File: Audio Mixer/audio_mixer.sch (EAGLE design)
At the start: 0 parts

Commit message: Audio Mixer half done
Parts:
- added C1, C2, C22, C23, C24, C25, C3, C31, C33, C34, C35, C4, C5, C6, C7, C8: 0.1u, rcl:C-EU025-030X050
- added C10, C11, C12, C9: 10u, rcl:CPOL-EUE5-10.5
- added C13, C14: 15n, rcl:C-EU025-030X050
- added C15: 100u, rcl:CPOL-EUE5-10.5
- added C16, C19, C20, C21: 2.2u, rcl:CPOL-EUE2.5-6
- added C17, C18: 56n, rcl:C-EU025-030X050
- added C26, C27, C28, C29: 47n, rcl:C-EU025-030X050
- added C30, C32: 1000u, rcl:C-EU050-050X075
- added IC1: LM747H, linear:LM747H
- added R1, R10, R11, R12, R13, R14, R15, R16, R17, R18, R19, R2, R20, R3, R4, R5, R6, R7, R8, R9: (no value), rcl:R-EU_R0805
- added R21, R22, R23, R24, R25, R26, R27, R28, R29, R30: (no value), rcl:POTENTIOMETER_PT-10
- added U1: TDA1524A, TDA1524A:TDA1524A
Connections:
- new net +12V: C11.+, IC1A.V+, IC1B.V+
- new net -12V: C10.-, C9.-, IC1P.V-
- new net AGND: C11.-, C9.+
- new net N$1: C1.1, R1.1
- new net N$10: R1.2, R21.3
- new net N$11: R2.2, R22.3
- new net N$12: R23.3, R3.2
- new net N$13: R24.3, R4.2
- new net N$14: R25.3, R5.2
- new net N$15: R26.3, R6.2
- new net N$16: R27.3, R7.2
- new net N$17: R28.3, R8.2
- new net N$18: C12.+, R10.1, R9.1
- new net N$19: IC1A.OUT, R10.2, R29.3
- new net N$2: C10.+, IC1A.+IN, IC1B.+IN, R21.2, R22.2, R23.2, R24.2, R25.2, R26.2, R27.2, R28.2
- new net N$20: IC1A.-IN, R21.1, R22.1, R23.1, R24.1, R29.1
- new net N$21: IC1B.-IN, R25.1, R26.1, R27.1, R28.1, R30.2
- new net N$22: IC1B.OUT, R30.3, R9.2
- new net N$23: C12.-, U1.LEFT_IN, U1.RIGHT_IN
- new net N$3: C2.1, R2.1
- new net N$4: C3.1, R3.1
- new net N$5: C4.1, R4.1
- new net N$6: C5.1, R5.1
- new net N$7: C6.1, R6.1
- new net N$8: C7.1, R7.1
- new net N$9: C8.1, R8.1

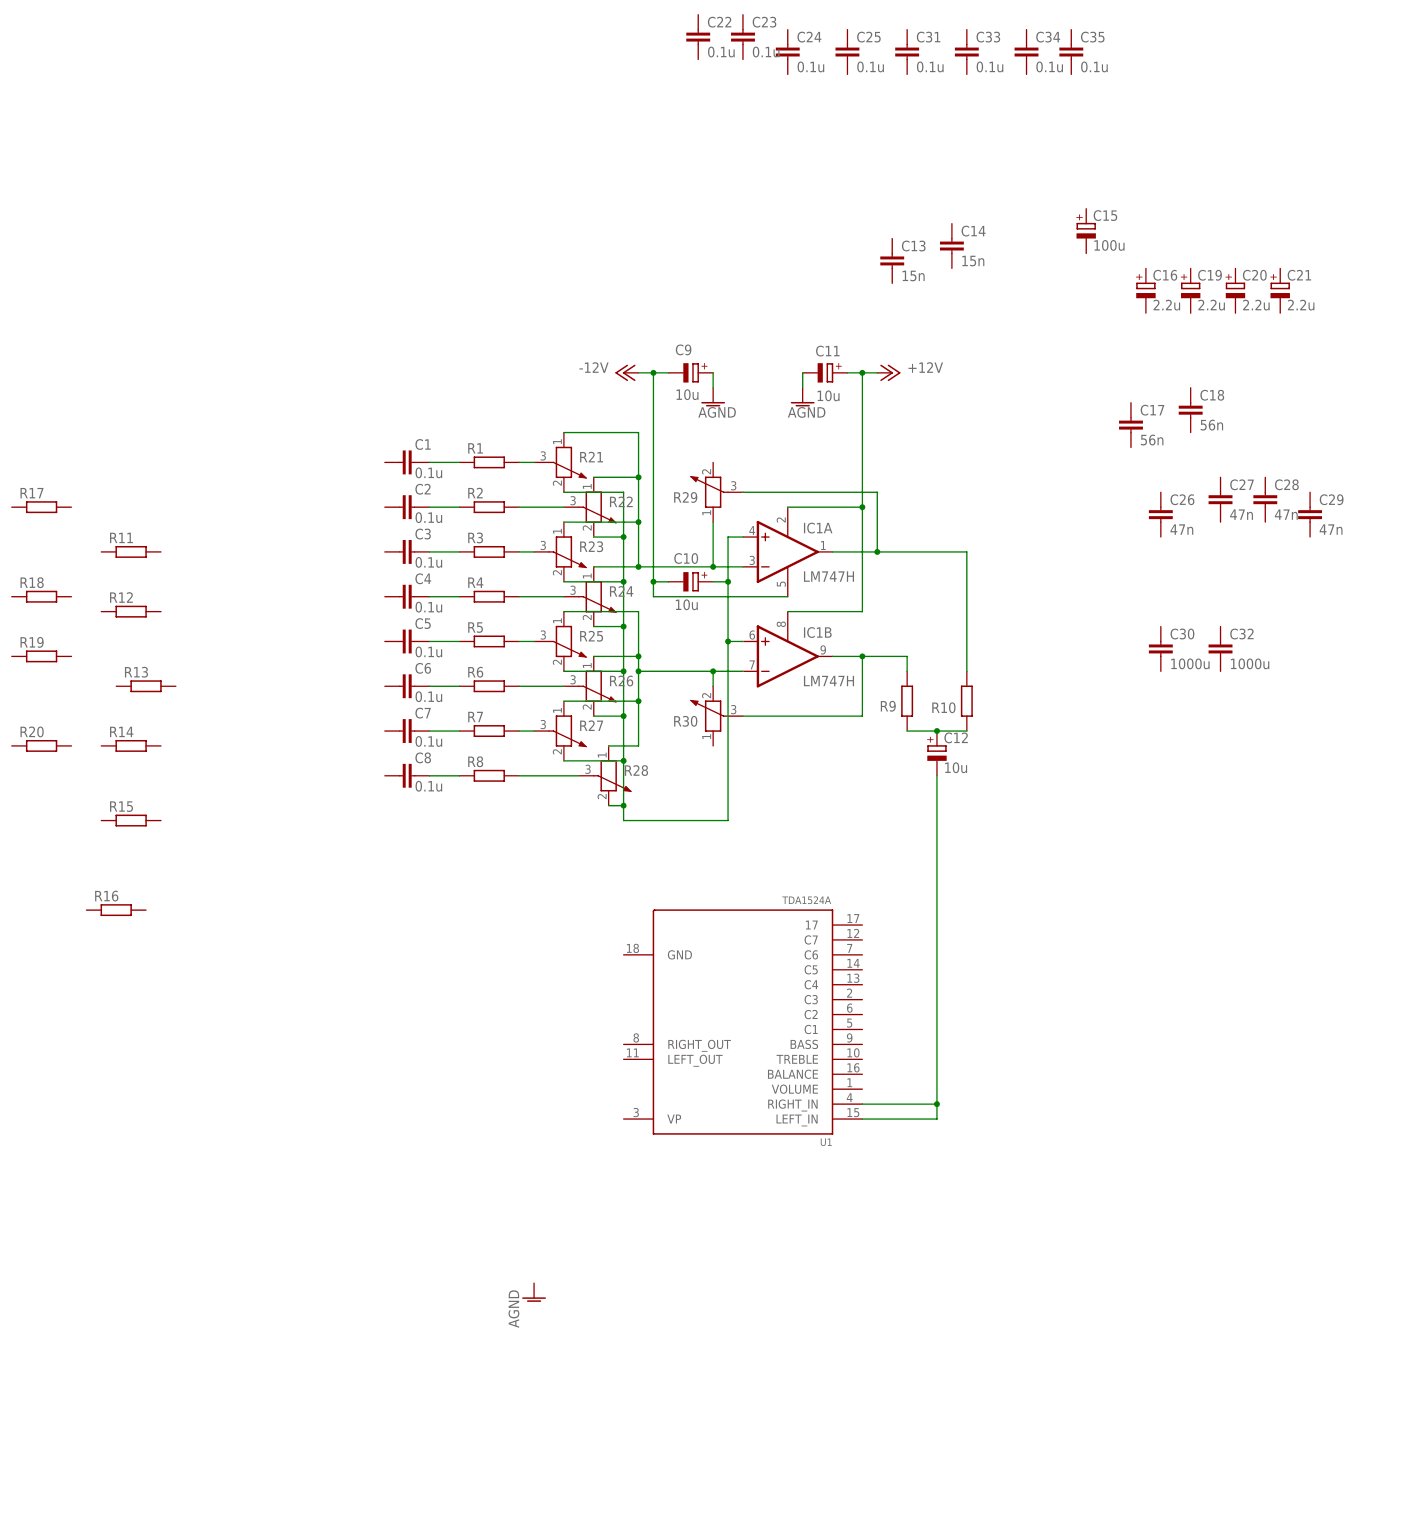
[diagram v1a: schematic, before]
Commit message: mixer schematic functionally done, todo labels and brd
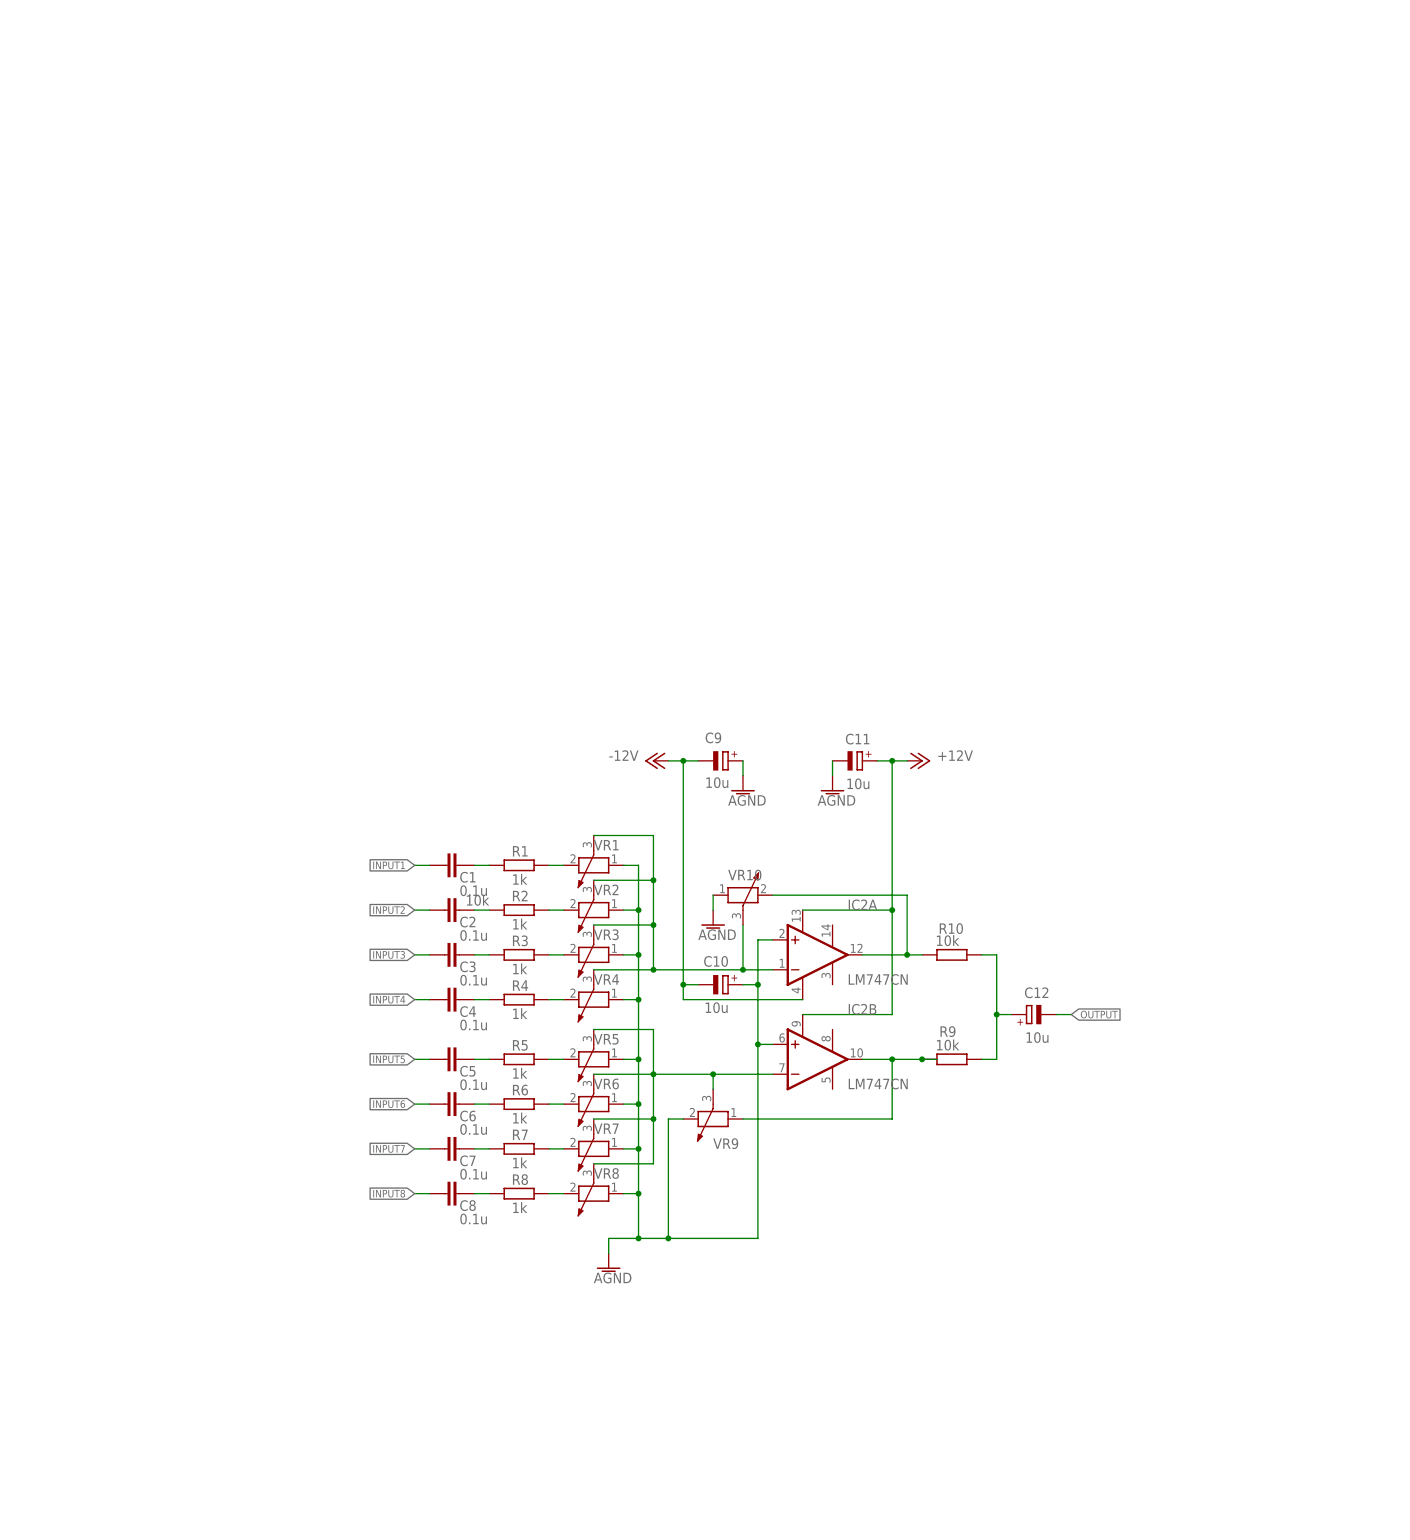
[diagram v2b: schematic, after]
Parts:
- removed C13, C14: 15n, rcl:C-EU025-030X050
- removed C15: 100u, rcl:CPOL-EUE5-10.5
- removed C16, C19, C20, C21: 2.2u, rcl:CPOL-EUE2.5-6
- removed C17, C18: 56n, rcl:C-EU025-030X050
- removed C22, C23, C24, C25, C31, C33, C34, C35: 0.1u, rcl:C-EU025-030X050
- removed C26, C27, C28, C29: 47n, rcl:C-EU025-030X050
- removed C30, C32: 1000u, rcl:C-EU050-050X075
- removed IC1: LM747H, linear:LM747H
- removed R11, R12, R13, R14, R15, R16, R17, R18, R19, R20: (no value), rcl:R-EU_R0805
- removed R21, R22, R23, R24, R25, R26, R27, R28, R29, R30: (no value), rcl:POTENTIOMETER_PT-10
- removed U1: TDA1524A, TDA1524A:TDA1524A
- added IC2: LM747CN, linear:LM747CN
- added VR1: 10k, rcl:POTENTIOMETER_PT-10
- added VR10, VR2, VR3, VR4, VR5, VR6, VR7, VR8, VR9: (no value), rcl:POTENTIOMETER_PT-10
- R1, R2, R3, R4, R5, R6, R7, R8: value (none) -> 1k
- R10, R9: value (none) -> 10k
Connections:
- removed net N$2 (its old number): C10.+, IC1A.+IN, IC1B.+IN, R21.2, R22.2, R23.2, R24.2, R25.2, R26.2, R27.2, R28.2
- removed net N$20: IC1A.-IN, R21.1, R22.1, R23.1, R24.1, R29.1
- removed net N$23: C12.-, U1.LEFT_IN, U1.RIGHT_IN
- new net INPUT1: C1.2
- new net INPUT2: C2.2
- new net INPUT3: C3.2
- new net INPUT4: C4.2
- new net INPUT5: C5.2
- new net INPUT6: C6.2
- new net INPUT7: C7.2
- new net INPUT8: C8.2
- new net N$18: R2.2, VR2.2
- new net OUTPUT: C12.-
- net +12V: now also IC2A.V+, IC2B.V+; no longer IC1A.V+, IC1B.V+
- net -12V: now also IC2P.V-; no longer IC1P.V-
- net AGND: now also C10.+, IC2A.+IN, IC2B.+IN, VR1.1, VR10.1, VR2.1, VR3.1, VR4.1, VR5.1, VR6.1, VR7.1, VR8.1, VR9.2
- net N$10: now also R3.2, VR3.2; no longer R1.2, R21.3
- net N$11: now also IC2B.-IN, VR5.3, VR6.3, VR7.3, VR8.3, VR9.3; no longer R2.2, R22.3
- net N$12: now also IC2A.-IN, VR1.3, VR10.3, VR2.3, VR3.3, VR4.3; no longer R23.3, R3.2
- net N$13: now also R1.2, VR1.2; no longer R24.3, R4.2
- net N$14: now also R4.2, VR4.2; no longer R25.3, R5.2
- net N$15: now also R5.2, VR5.2; no longer R26.3, R6.2
- net N$16: now also R6.2, VR6.2; no longer R27.3, R7.2
- net N$17: now also R7.2, VR7.2; no longer R28.3, R8.2
- net N$19: now also IC2A.OUT, VR10.2; no longer IC1A.OUT, R29.3
- net N$21: now also R8.2, VR8.2; no longer IC1B.-IN, R25.1, R26.1, R27.1, R28.1, R30.2
- net N$22: now also IC2B.OUT, VR9.1; no longer IC1B.OUT, R30.3
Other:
- moved on the sheet: C1, C10, C11, C12, C2, C3, C4, C5, C6, C7, C8, C9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

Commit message: Mixer Design complete
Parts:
- removed IC2: LM747CN, linear:LM747CN
- added C13: 10u, rcl:CPOL-EUE5-10.5
- added C14, C15, C16, C17, C18, C19, C20, C21, C22, C24: 0.1u, rcl:C-EU025-030X050
- added IC1: OPA2134P, linear:OPA2134P
- added INPUT_AUDIO: (no value), pinhead:PINHD-2X9
- added OUTPUT_AUDIO, POWER: (no value), pinhead:PINHD-1X3
- added R11, R12, R13, R14, R15, R16, R17, R18, R19, R21: 1k, rcl:R-EU_R0805
- added VR11, VR16: 10k, rcl:POTENTIOMETER_PT-10
- added VR12, VR13, VR14, VR15, VR17, VR18, VR19, VR21: (no value), rcl:POTENTIOMETER_PT-10
- VR6: value (none) -> 10k
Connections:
- removed net +12V: C11.+, IC2A.V+, IC2B.V+
- removed net -12V: C10.-, C9.-, IC2P.V-
- removed net INPUT1: C1.2
- removed net INPUT2: C2.2
- removed net INPUT3: C3.2
- removed net INPUT4: C4.2
- removed net INPUT5: C5.2
- removed net INPUT6: C6.2
- removed net INPUT7: C7.2
- removed net INPUT8: C8.2
- removed net OUTPUT: C12.-
- new net +15V: C11.+, IC1P.V+, POWER.1
- new net -15V: C10.-, C9.-, IC1P.V-, POWER.2
- new net L_INPUT1: C15.2, INPUT_AUDIO.1
- new net L_INPUT2: C16.2, INPUT_AUDIO.3
- new net L_INPUT3: C17.2, INPUT_AUDIO.5
- new net L_INPUT4: C18.2, INPUT_AUDIO.7
- new net L_INPUT5: C19.2, INPUT_AUDIO.9
- new net L_INPUT6: C20.2, INPUT_AUDIO.11
- new net L_INPUT7: C21.2, INPUT_AUDIO.13
- new net L_INPUT8: C22.2, INPUT_AUDIO.15
- new net N$20: C13.+, R9.1
- new net N$23: R13.2, VR7.2
- new net N$24: VR1.1, VR2.1, VR3.1, VR4.1
- new net N$28: R7.2, VR13.2
- new net N$29: R5.2, VR11.2
- new net N$30: R6.2, VR12.2
- new net N$32: R8.2, VR14.2
- new net N$34: VR11.1, VR12.1, VR13.1, VR14.1, VR15.1, VR5.1, VR6.1, VR7.1, VR8.1
- new net N$35: C18.1, R15.1
- new net N$36: R15.2, VR15.2
- new net N$37: IC1B.-IN, VR15.3, VR16.3, VR17.3, VR18.3, VR19.3, VR21.3, VR6.3, VR7.3, VR8.3, VR9.3
- new net N$39: C19.1, R16.1
- new net N$40: C20.1, R17.1
- new net N$41: C21.1, R18.1
- new net N$42: R18.2, VR18.2
- new net N$43: R16.2, VR16.2
- new net N$44: R17.2, VR17.2
- new net N$45: C22.1, R19.1
- new net N$46: R19.2, VR19.2
- new net N$6: C14.1, R11.1
- new net N$7: R11.2, VR5.2
- new net N$8: C24.1, R21.1
- new net N$9: R21.2, VR21.2
- new net OUTPUT_L: C13.-, OUTPUT_AUDIO.1
- new net OUTPUT_R: C12.-, OUTPUT_AUDIO.2
- new net R_INPUT1: C1.2, INPUT_AUDIO.2
- new net R_INPUT2: C2.2, INPUT_AUDIO.4
- new net R_INPUT3: C3.2, INPUT_AUDIO.6
- new net R_INPUT4: C4.2, INPUT_AUDIO.8
- new net R_INPUT5: C5.2, INPUT_AUDIO.10
- new net R_INPUT6: C6.2, INPUT_AUDIO.12
- new net R_INPUT7: C7.2, INPUT_AUDIO.14
- new net R_INPUT8: C8.2, INPUT_AUDIO.16
- new net TEENSY_L: C24.2, INPUT_AUDIO.17
- new net TEENSY_R: C14.2, INPUT_AUDIO.18
- net AGND: now also IC1A.+IN, IC1B.+IN, OUTPUT_AUDIO.3, POWER.3, VR16.1, VR17.1, VR18.1, VR19.1; no longer IC2A.+IN, IC2B.+IN, VR1.1, VR2.1, VR3.1, VR4.1, VR5.1, VR6.1, VR7.1, VR8.1
- net N$11: now also C15.1, R12.1; no longer IC2B.-IN, VR5.3, VR6.3, VR7.3, VR8.3, VR9.3
- net N$12: now also IC1A.-IN, VR11.3, VR12.3, VR13.3, VR14.3, VR5.3; no longer IC2A.-IN
- net N$15: now also C16.1, R13.1; no longer R5.2, VR5.2
- net N$16: now also C17.1, R14.1; no longer R6.2, VR6.2
- net N$17: now also R14.2, VR8.2; no longer R7.2, VR7.2
- net N$19: now also IC1A.OUT; no longer IC2A.OUT
- net N$2: no longer R9.1
- net N$21: now also R12.2, VR6.2; no longer R8.2, VR8.2
- net N$22: now also IC1B.OUT; no longer IC2B.OUT
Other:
- note added: "Audio inputs. MIC level"
- note added: "LEFT Gain control"
- note added: "Level adj, weight control"
- note added: "RIGHT Gain control"
- note added: "To pre-amp"
- moved on the sheet: C1, C10, C11, C12, C2, C3, C4, C5, C6, C7, C8, C9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

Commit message: audio mixer comlpete!
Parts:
- removed C24: 0.1u, rcl:C-EU025-030X050
- removed R21: 1k, rcl:R-EU_R0805
- removed VR21: (no value), rcl:POTENTIOMETER_PT-10
- added C23: 10u, rcl:CPOL-EUE5-10.5
- added R20: 10k, rcl:R-EU_R0805
- added VR20: EVUF2A, pot:EVUF2A
- C10, C11, C12, C13, C9: value 10u -> 0.1u; device rcl:CPOL-EUE5-10.5 -> rcl:C-EU025-030X050
- C19, C20, C21, C22: value 0.1u -> 10u; device rcl:C-EU025-030X050 -> rcl:CPOL-EUE5-10.5
- R10, R9: value 10k -> 1k
- R19: value 1k -> 10k
- VR1, VR11, VR16, VR6: value 10k -> EVUF2A; device rcl:POTENTIOMETER_PT-10 -> pot:EVUF2A
- VR10, VR12, VR13, VR14, VR15, VR17, VR18, VR19, VR2, VR3, VR4, VR5, VR7, VR8, VR9: value (none) -> EVUF2A; device rcl:POTENTIOMETER_PT-10 -> pot:EVUF2A
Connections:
- removed net N$12: IC1A.-IN, VR1.3, VR10.3, VR11.3, VR12.3, VR13.3, VR14.3, VR2.3, VR3.3, VR4.3, VR5.3
- removed net N$19: IC1A.OUT, R10.2, VR10.2
- removed net N$22: IC1B.OUT, R9.2, VR9.1
- removed net N$24: VR1.1, VR2.1, VR3.1, VR4.1
- removed net N$34: VR11.1, VR12.1, VR13.1, VR14.1, VR15.1, VR5.1, VR6.1, VR7.1, VR8.1
- removed net N$37: IC1B.-IN, VR15.3, VR16.3, VR17.3, VR18.3, VR19.3, VR21.3, VR6.3, VR7.3, VR8.3, VR9.3
- new net LEFT_OP_OUT: IC1B.OUT, R20.2, VR20.A
- new net L_OP_IN: IC1B.-IN, VR10.S, VR11.S, VR12.S, VR13.S, VR14.S, VR15.S, VR16.S, VR17.S, VR18.S, VR20.S
- new net RIGHT_OP_OUT: IC1A.OUT, R19.2, VR19.A
- new net R_OP_IN: IC1A.-IN, VR1.S, VR19.S, VR2.S, VR3.S, VR4.S, VR5.S, VR6.S, VR7.S, VR8.S, VR9.S
- net +15V: now also C20.+; no longer C11.+
- net -15V: now also C19.-, C21.-; no longer C10.-, C9.-
- net AGND: now also C19.+, C20.-, C21.+, VR1.E, VR10.E, VR11.E, VR12.E, VR13.E, VR14.E, VR15.E, VR16.E, VR17.E, VR18.E, VR19.E, VR2.E, VR20.E, VR3.E, VR4.E, VR5.E, VR6.E, VR7.E, VR8.E, VR9.E; no longer C10.+, C11.-, C9.+, VR10.1, VR16.1, VR17.1, VR18.1, VR19.1, VR9.2
- net L_INPUT1: now also C10.2; no longer C15.2
- net L_INPUT2: now also C11.2; no longer C16.2
- net L_INPUT3: now also C12.2; no longer C17.2
- net L_INPUT4: now also C13.2; no longer C18.2
- net L_INPUT5: now also C14.2; no longer C19.2
- net L_INPUT6: now also C15.2; no longer C20.2
- net L_INPUT7: now also C16.2; no longer C21.2
- net L_INPUT8: now also C17.2; no longer C22.2
- net N$10: now also VR3.A; no longer VR3.2
- net N$11: now also C11.1, R11.1; no longer C15.1, R12.1
- net N$13: now also VR1.A; no longer VR1.2
- net N$14: now also VR4.A; no longer VR4.2
- net N$15: now also C12.1, R12.1; no longer C16.1, R13.1
- net N$16: now also C13.1, R13.1; no longer C17.1, R14.1
- net N$17: now also R13.2, VR13.A; no longer R14.2, VR8.2
- net N$18: now also VR2.A; no longer VR2.2
- net N$2: now also C22.+, R19.1; no longer C12.+, R10.1
- net N$20: now also C23.+, R20.1; no longer C13.+, R9.1
- net N$21: now also R11.2, VR11.A; no longer R12.2, VR6.2
- net N$23: now also R12.2, VR12.A; no longer R13.2, VR7.2
- net N$28: now also VR7.A; no longer VR13.2
- net N$29: now also VR5.A; no longer VR11.2
- net N$30: now also VR6.A; no longer VR12.2
- net N$32: now also VR8.A; no longer VR14.2
- net N$35: now also C14.1, R14.1; no longer C18.1, R15.1
- net N$36: now also R14.2, VR14.A; no longer R15.2, VR15.2
- net N$39: now also C15.1, R15.1; no longer C19.1, R16.1
- net N$40: now also C16.1, R16.1; no longer C20.1, R17.1
- net N$41: now also C17.1, R17.1; no longer C21.1, R18.1
- net N$42: now also R17.2, VR17.A; no longer R18.2, VR18.2
- net N$43: now also R15.2, VR15.A; no longer R16.2, VR16.2
- net N$44: now also R16.2, VR16.A; no longer R17.2, VR17.2
- net N$45: now also C18.1, R18.1; no longer C22.1, R19.1
- net N$46: now also R18.2, VR18.A; no longer R19.2, VR19.2
- net N$6: now also C9.1, R9.1; no longer C14.1, R11.1
- net N$7: now also R9.2, VR9.A; no longer R11.2, VR5.2
- net N$8: now also C10.1, R10.1; no longer C24.1, R21.1
- net N$9: now also R10.2, VR10.A; no longer R21.2, VR21.2
- net OUTPUT_L: now also C23.-; no longer C13.-
- net OUTPUT_R: now also C22.-; no longer C12.-
- net TEENSY_L: now also C18.2; no longer C24.2
- net TEENSY_R: now also C9.2; no longer C14.2
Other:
- note added: "LEFT Gain control >VALUE: 1M Note: Should be linear tapered for gain adjustment"
- note added: "Level adj, weight control: >VALUE: 10K Note: Should be Log tapered for Audio"
- note added: "RIGHT Gain control >VALUE: 1M Note: Should be linear tapered for gain adjustment"
- note removed: "LEFT Gain control"
- note removed: "Level adj, weight control"
- note removed: "RIGHT Gain control"
- moved on the sheet: C14, C15, C16, C17, C18, R10, R11, R12, R13, R14, R15, R16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

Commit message: old seperate files
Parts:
- VR1, VR10, VR11, VR12, VR13, VR14, VR15, VR16, VR17, VR18, VR2, VR3, VR4, VR5, VR6, VR7, VR8, VR9: value EVUF2A -> (none); device pot:EVUF2A -> rcl:R-TRIMM3339P
